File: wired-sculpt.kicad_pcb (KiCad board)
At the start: 2 copper layers, 40 x 54 mm, 39 parts, among them J1 10103594-0001LF, J2 FFC3B07-30-T, J3 AVR-ISP-6 - NOT FITTED, Q1 BSS84AK,215, Q2 2N7002BK,215, SW1 FSMSM, SW2 S2B-PH-K-S(LF)(SN), U1 USBLC6-2SC6, U2 LM2776DBVT, U3 AT90USB1286-AUR, Y1 TSX-3225 16.0000MF18X-AC0

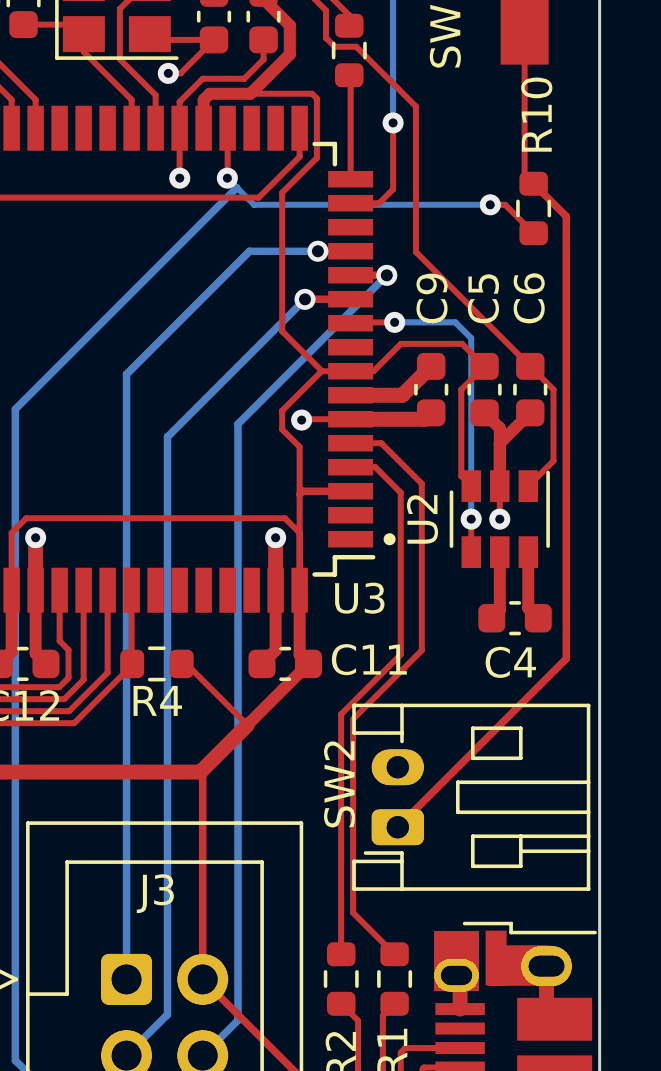
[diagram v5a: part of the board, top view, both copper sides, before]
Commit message: Remove reset switch header
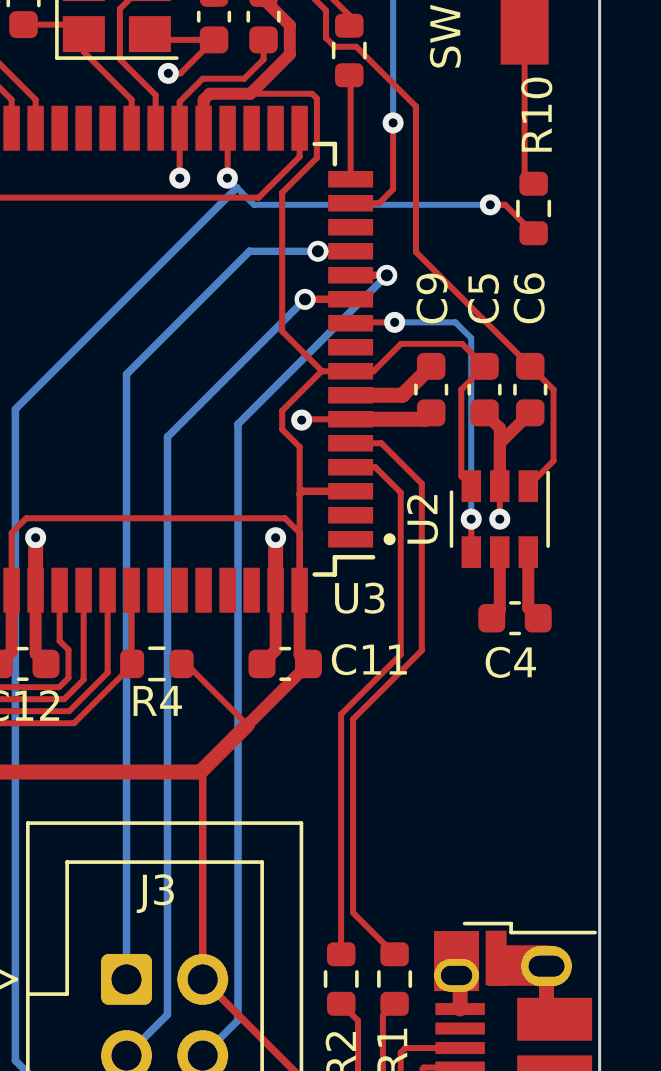
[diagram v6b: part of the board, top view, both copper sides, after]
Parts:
- removed SW2: S2B-PH-K-S(LF)(SN), Connector_JST:JST_PH_S2B-PH-K_1x02_P2.00mm_Horizontal
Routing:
- net Net-(R10-Pad2): track 29.4 -> 5.18 mm
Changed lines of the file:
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@@
-    )
-  )
-  (footprint "Connector_JST:JST_PH_S2B-PH-K_1x02_P2.00mm_Horizontal" (layer "F.Cu")
-    (at 153.271953 67.600023 90)
-    (descr "JST PH series connector, S2B-PH-K (http://www.jst-mfg.com/product/pdf/eng/ePH.pdf), generated with kicad-footprint-generator")
-    (tags "connector JST PH top entry")
-    (property "MPN" "S2B-PH-K-S(LF)(SN)")
-    (property "Notes" "JST connector")
-    (property "Sheetfile" "wired-sculpt.kicad_sch")
-    (property "Sheetname" "")
-    (attr through_hole)
-    (fp_text reference "SW2" (at 1.453444 -1.904499 90) (layer "F.SilkS")
-      (effects (font (size 1 1) (thickness 0.15)))
-    )
-    (fp_text value "S2B-PH-K-S(LF)(SN)" (at 1 7.45 90) (layer "F.Fab")
-      (effects (font (size 1 1) (thickness 0.15)))
-    )
-    (fp_text user "${REFERENCE}" (at 1 2.5 90) (layer "F.Fab")
-      (effects (font (size 1 1) (thickness 0.15)))
-    )
-    (fp_line (start -0.8 4.1) (end -0.8 6.36) (layer "F.SilkS") (width 0.12))
-    (fp_line (start 2.3 4.1) (end 2.3 2.5) (layer "F.SilkS") (width 0.12))
-    (fp_line (start 2.3 2.5) (end 3.3 2.5) (layer "F.SilkS") (width 0.12))
-    (fp_line (start -1.14 -1.46) (end -2.06 -1.46) (layer "F.SilkS") (width 0.12))
-    (fp_line (start 3.3 2.5) (end 3.3 4.1) (layer "F.SilkS") (width 0.12))
-    (fp_line (start -0.86 0.14) (end -1.14 0.14) (layer "F.SilkS") (width 0.12))
-    (fp_line (start -0.86 0.14) (end -0.86 -1.075) (layer "F.SilkS") (width 0.12))
-    (fp_line (start 0.5 6.36) (end 0.5 2) (layer "F.SilkS") (width 0.12))
-    (fp_line (start -0.3 2.5) (end -1.3 2.5) (layer "F.SilkS") (width 0.12))
-    (fp_line (start 4.06 0.14) (end 3.14 0.14) (layer "F.SilkS") (width 0.12))
-    (fp_line (start -1.3 2.5) (end -1.3 4.1) (layer "F.SilkS") (width 0.12))
-    (fp_line (start 1.5 2) (end 1.5 6.36) (layer "F.SilkS") (width 0.12))
-    (fp_line (start -2.06 -1.46) (end -2.06 6.36) (layer "F.SilkS") (width 0.12))
-    (fp_line (start 0.5 2) (end 1.5 2) (layer "F.SilkS") (width 0.12))
-    (fp_line (start 3.3 4.1) (end 2.3 4.1) (layer "F.SilkS") (width 0.12))
-    (fp_line (start 4.06 6.36) (end 4.06 -1.46) (layer "F.SilkS") (width 0.12))
-    (fp_line (start -2.06 0.14) (end -1.14 0.14) (layer "F.SilkS") (width 0.12))
-    (fp_line (start -2.06 6.36) (end 4.06 6.36) (layer "F.SilkS") (width 0.12))
-    (fp_line (start -0.3 4.1) (end -0.3 6.36) (layer "F.SilkS") (width 0.12))
-    (fp_line (start 4.06 -1.46) (end 3.14 -1.46) (layer "F.SilkS") (width 0.12))
-    (fp_line (start -1.14 0.14) (end -1.14 -1.46) (layer "F.SilkS") (width 0.12))
-    (fp_line (start -1.3 4.1) (end -0.3 4.1) (layer "F.SilkS") (width 0.12))
-    (fp_line (start 3.14 0.14) (end 2.86 0.14) (layer "F.SilkS") (width 0.12))
-    (fp_line (start 3.14 -1.46) (end 3.14 0.14) (layer "F.SilkS") (width 0.12))
-    (fp_line (start -0.3 4.1) (end -0.3 2.5) (layer "F.SilkS") (width 0.12))
-    (fp_line (start 4.45 -1.85) (end -2.45 -1.85) (layer "F.CrtYd") (width 0.05))
-    (fp_line (start -2.45 -1.85) (end -2.45 6.75) (layer "F.CrtYd") (width 0.05))
-    (fp_line (start -2.45 6.75) (end 4.45 6.75) (layer "F.CrtYd") (width 0.05))
-    (fp_line (start 4.45 6.75) (end 4.45 -1.85) (layer "F.CrtYd") (width 0.05))
-    (fp_line (start 0.5 1.375) (end 0 0.875) (layer "F.Fab") (width 0.1))
-    (fp_line (start -1.25 0.25) (end -1.25 -1.35) (layer "F.Fab") (width 0.1))
-    (fp_line (start 3.25 -1.35) (end 3.25 0.25) (layer "F.Fab") (width 0.1))
-    (fp_line (start 3.95 6.25) (end 3.95 -1.35) (layer "F.Fab") (width 0.1))
-    (fp_line (start 3.95 -1.35) (end 3.25 -1.35) (layer "F.Fab") (width 0.1))
-    (fp_line (start -1.25 -1.35) (end -1.95 -1.35) (layer "F.Fab") (width 0.1))
-    (fp_line (start -0.5 1.375) (end 0.5 1.375) (layer "F.Fab") (width 0.1))
-    (fp_line (start 0 0.875) (end -0.5 1.375) (layer "F.Fab") (width 0.1))
-    (fp_line (start -1.95 6.25) (end 3.95 6.25) (layer "F.Fab") (width 0.1))
-    (fp_line (start -1.95 -1.35) (end -1.95 6.25) (layer "F.Fab") (width 0.1))
-    (fp_line (start 3.25 0.25) (end -1.25 0.25) (layer "F.Fab") (width 0.1))
-    (pad "1" thru_hole roundrect locked (at 0 0 90) (size 1.2 1.75) (drill 0.75) (layers *.Cu *.Mask) (roundrect_rratio 0.2083325)
-      (net 57 "Net-(R10-Pad2)") (pinfunction "Pin_1") (pintype "passive"))
-    (pad "2" thru_hole oval locked (at 2 0 90) (size 1.2 1.75) (drill 0.75) (layers *.Cu *.Mask)
-      (net 1 "GND") (pinfunction "Pin_2") (pintype "passive"))
-    (model "${KISYS3DMOD}/Connector_JST.3dshapes/JST_PH_S2B-PH-K_1x02_P2.00mm_Horizontal.wrl"
-      (offset (xyz 0 0 0))
-      (scale (xyz 1 1 1))
-      (rotate (xyz 0 0 0))
     )
   )
@@
   (segment (start 137.350001 58.515001) (end 137.350001 54.100001) (width 0.2) (layer "F.Cu") (net 56))
   (segment (start 134.625 60) (end 135.975001 58.649999) (width 0.2) (layer "F.Cu") (net 56))
-  (segment (start 158.887529 61.984447) (end 158.88753 47.23753) (width 0.25) (layer "F.Cu") (net 57))
   (segment (start 157.5 45.85) (end 157.8 46.15) (width 0.2) (layer "F.Cu") (net 57))
-  (segment (start 158.88753 47.23753) (end 157.8 46.15) (width 0.25) (layer "F.Cu") (net 57))
-  (segment (start 153.271953 67.600023) (end 158.887529 61.984447) (width 0.25) (layer "F.Cu") (net 57))
   (segment (start 157.5 41.09) (end 157.5 45.85) (width 0.2) (layer "F.Cu") (net 57))
   (segment (start 130.675 39.575) (end 129.25 41) (width 0.25) (layer "F.Cu") (net 72))

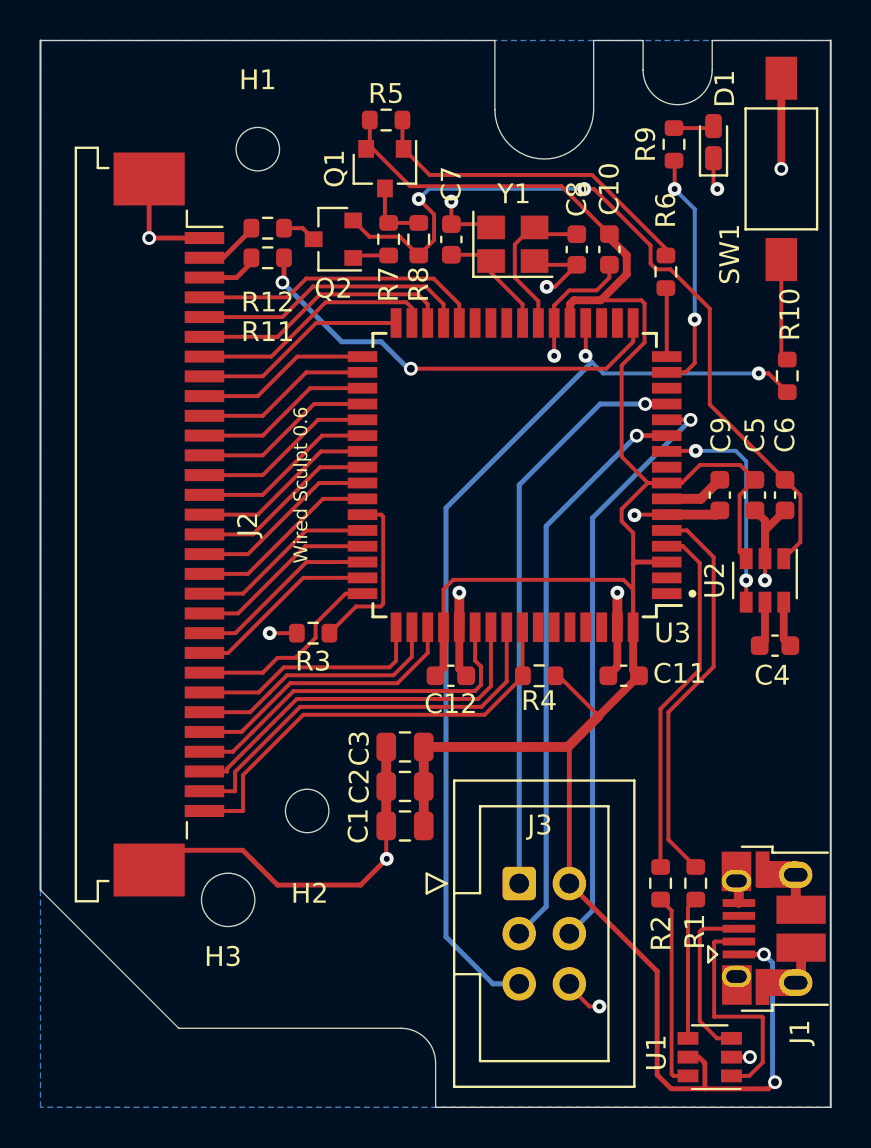
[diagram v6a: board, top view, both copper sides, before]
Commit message: Change connector to USB-C
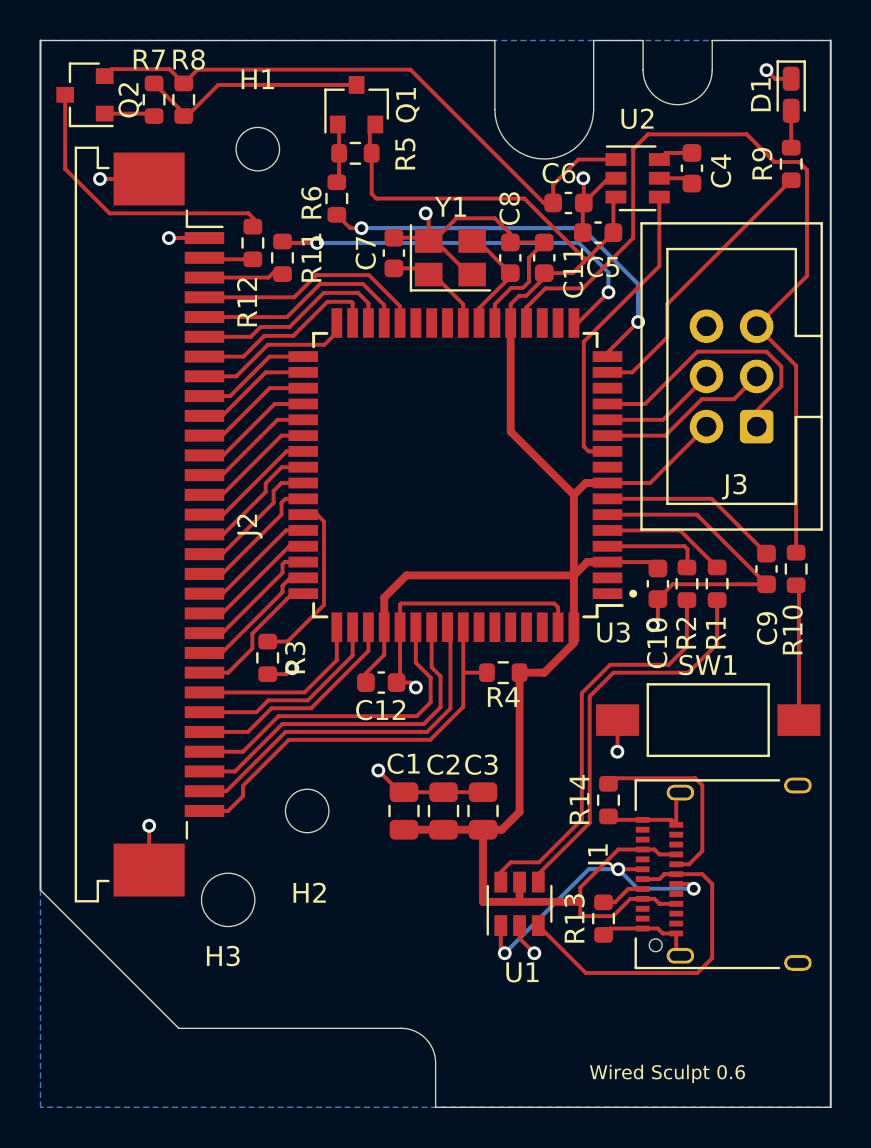
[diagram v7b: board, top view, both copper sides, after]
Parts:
- added R13: ERJ-3EKF5101V, Resistor_SMD:R_0603_1608Metric, F.Cu at (148.5, 74.5)
- added R14: ERJ-3EKF5101V, Resistor_SMD:R_0603_1608Metric, F.Cu at (148.8, 68.5)
- J1: value 10103594-0001LF -> USB_C_Receptacle; footprint Connector_USB:USB_Micro-B_Amphenol_10103594-0001LF_Horizontal -> Connector_USB:USB_C_Receptacle_Amphenol_12401610E4-2A
- moved SW1 28.1 mm to (153.8, 64.4), turned to 0 degrees
- moved J3 26.1 mm to (156.3, 49.5), turned to 180 degrees
- moved C4 24.5 mm to (153.0, 36.5), turned to 90 degrees
- moved C11 21.5 mm to (145.5, 41.0), turned to -90 degrees
- moved U2 21.4 mm to (150.2, 37.0), turned to 0 degrees
- moved C6 18.4 mm to (146.7, 38.2), turned to 180 degrees
- moved C10 17.1 mm to (151.2, 57.5)
- moved R6 17.1 mm to (135.0, 38.0)
- moved C5 15.5 mm to (148.2, 39.7), turned to 0 degrees
- moved R2 15.2 mm to (152.7, 57.5)
- moved R1 15.2 mm to (154.2, 57.5)
- moved Q2 14.5 mm to (122.2, 32.8)
- moved R8 13.8 mm to (127.2, 33.0), turned to -90 degrees
- moved R7 13.8 mm to (125.8, 33.0)
- moved U1 12.4 mm to (144.2, 73.7), turned to 90 degrees
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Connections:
- U1 pad 1: /Din- -> Din-
- U1 pad 3: /Din+ -> Din+
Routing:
- net MOSI: track 29.8 -> 5.92 mm, vias 1 -> 0
- net SCK: track 29.2 -> 8.79 mm, vias 1 -> 0
- net Din+: track 0.00 -> 17.7 mm
- net GREEN+: track 3.42 -> 21.0 mm, vias 0 -> 2
- net VBUS: track 127.7 -> 110.4 mm, vias 2 -> 0
- net MISO: track 29.3 -> 13.8 mm, vias 1 -> 0
- net Din-: track 0.00 -> 15.4 mm, vias 0 -> 3
- net Net-(Q1-Pad1): track 17.1 -> 2.75 mm
- net /D+: track 20.1 -> 6.33 mm
- net /D-: track 18.2 -> 5.01 mm
- net GREEN-: track 1.73 -> 14.6 mm
- net /Dout+: track 7.19 -> 19.8 mm
- net /Din-: track 11.6 -> 0.00 mm
- net /Dout-: track 9.93 -> 20.8 mm
- net -5V: track 40.5 -> 30.9 mm, vias 2 -> 0
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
